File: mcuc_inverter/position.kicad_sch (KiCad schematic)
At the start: 0 parts

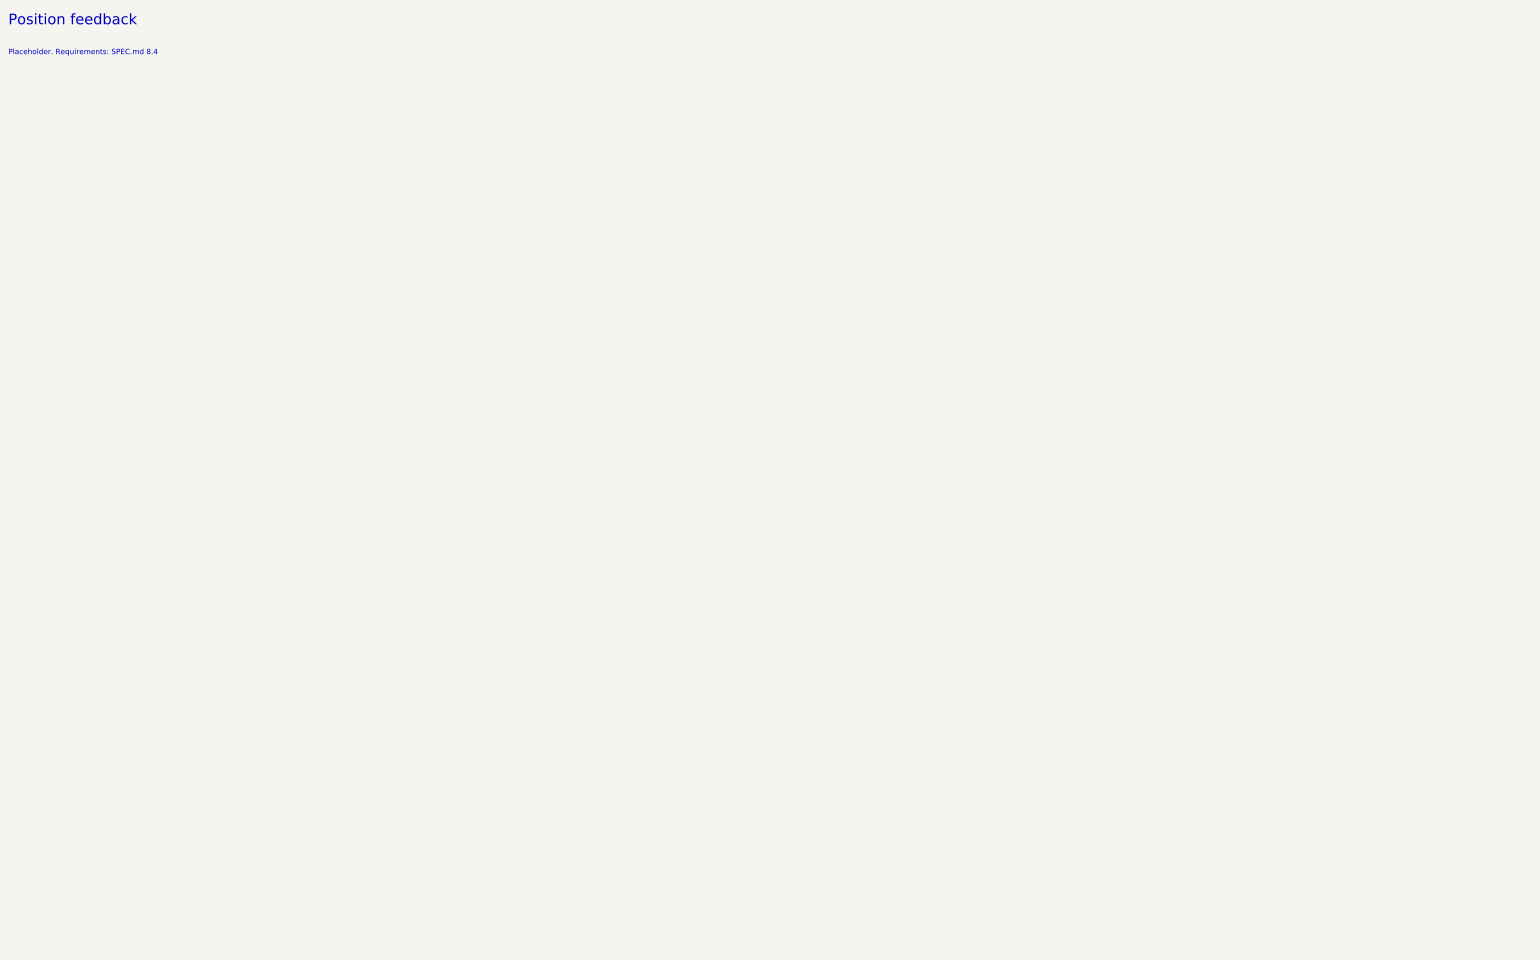
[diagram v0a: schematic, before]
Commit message: Capture position sheet: AD2S1205 resolver, halls, encoder, SinCos
Port from PALTA legacy sheets, verified pin-by-pin against the ADI
datasheet and the legacy VESC-controller.net (175/175 netlist
checks). Fixes two legacy defects found during reconstruction: SOE
(serial output enable, an INPUT mislabeled as output in the legacy
symbol) was left floating on PALTA - now tied low for serial mode;
and the A/B/NM encoder-emulation outputs that make VESC resolver
support free (D003) were never wired on the legacy board - now
brought out via 0R links with an exclusive-population note vs the
external ABI encoder. REFBYP decoupling added per datasheet (PALTA
floated pin 43).

Exciter (AD8397), hall clamps (10k + BAT54S, PALTA-faithful, DNP
pullup sites), encoder inputs replicating the hall pattern, SinCos
from the PALTA analog-input pattern, motor temp bias per D022
(resistor-selectable). APX809-46 5V supervisor for AD2S1205 RESET.
8 MHz -> 8.192 MHz crystal correction per datasheet nominal.

ERC 0 errors on root hierarchy.

Co-Authored-By: Claude Fable 5 <noreply@anthropic.com>
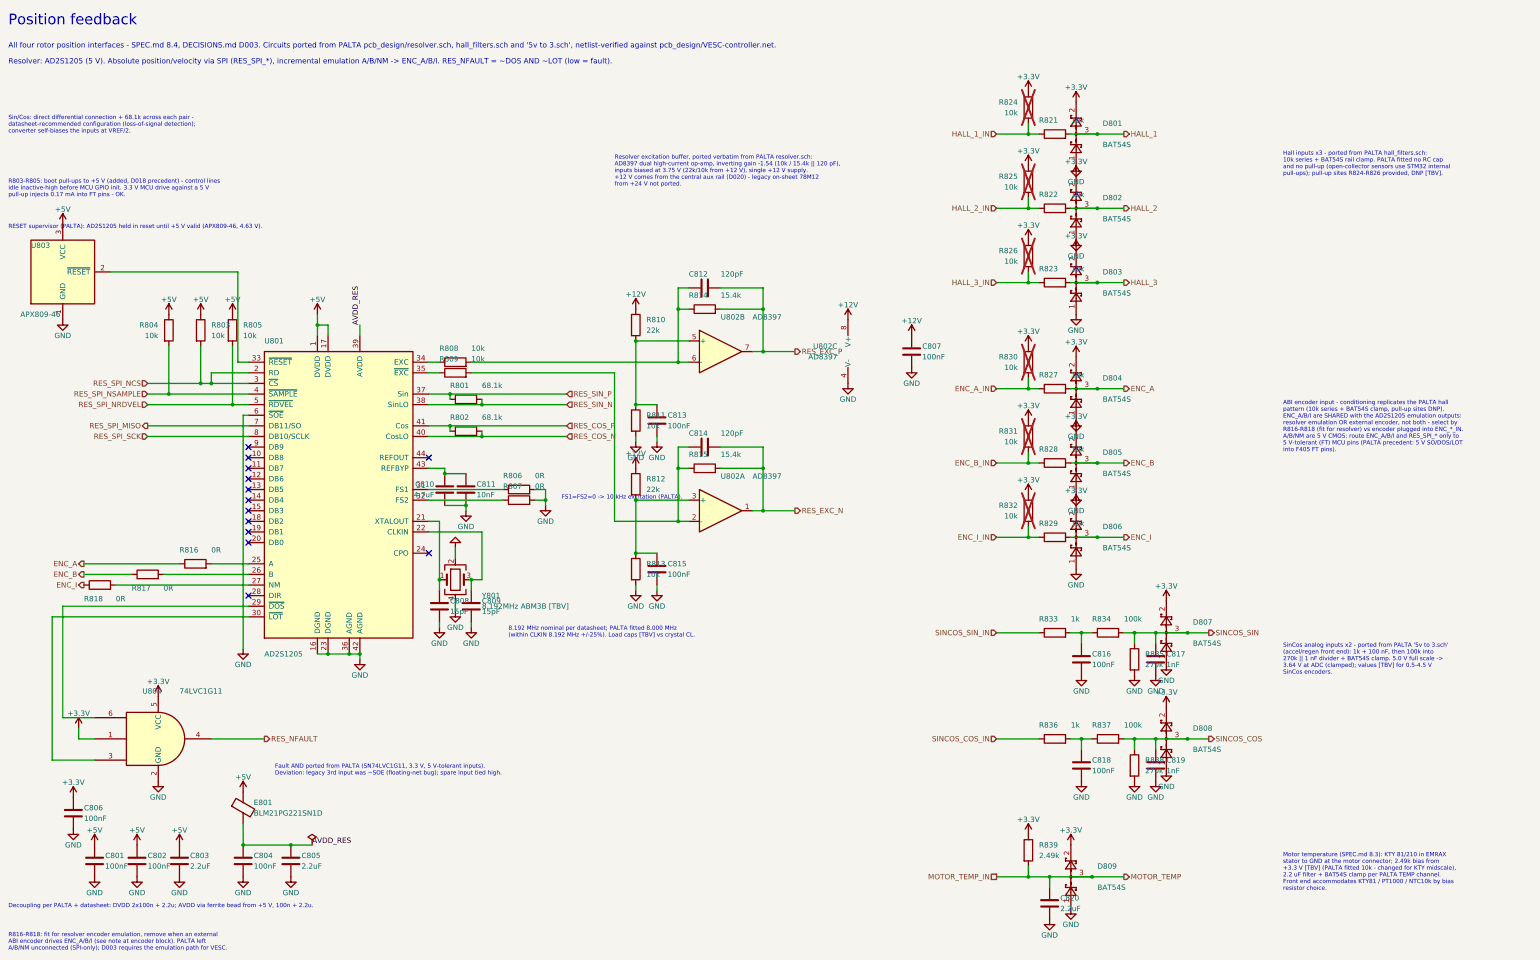
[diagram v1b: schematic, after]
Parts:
- added C801, C802, C804, C806, C807, C813, C815, C816, C818: 100nF, Capacitor_SMD:C_0603_1608Metric, symbol Device:C
- added C803, C805, C820: 2.2uF, Capacitor_SMD:C_0603_1608Metric, symbol Device:C
- added C808, C809: 15pF, Capacitor_SMD:C_0603_1608Metric, symbol Device:C
- added C810: 4.7uF, Capacitor_SMD:C_0603_1608Metric, symbol Device:C
- added C811: 10nF, Capacitor_SMD:C_0603_1608Metric, symbol Device:C
- added C812, C814: 120pF, Capacitor_SMD:C_0603_1608Metric, symbol Device:C
- added C817, C819: 1nF, Capacitor_SMD:C_0603_1608Metric, symbol Device:C
- added D801, D802, D803, D804, D805, D806, D807, D808, D809: BAT54S, Package_TO_SOT_SMD:SOT-23, symbol Diode:BAT54S
- added E801: BLM21PG221SN1D, Inductor_SMD:L_0805_2012Metric, symbol Device:FerriteBead
- added R801, R802: 68.1k, Resistor_SMD:R_0603_1608Metric, symbol Device:R
- added R803, R804, R805, R808, R809, R811, R813, R821, R822, R823, R824, R825, R826, R827, R828, R829, R830, R831, R832: 10k, Resistor_SMD:R_0603_1608Metric, symbol Device:R
- added R806, R807, R816, R817, R818: 0R, Resistor_SMD:R_0603_1608Metric, symbol Device:R
- added R810, R812: 22k, Resistor_SMD:R_0603_1608Metric, symbol Device:R
- added R814, R815: 15.4k, Resistor_SMD:R_0603_1608Metric, symbol Device:R
- added R833, R836: 1k, Resistor_SMD:R_0603_1608Metric, symbol Device:R
- added R834, R837: 100k, Resistor_SMD:R_0603_1608Metric, symbol Device:R
- added R835, R838: 270k, Resistor_SMD:R_0603_1608Metric, symbol Device:R
- added R839: 2.49k, Resistor_SMD:R_0603_1608Metric, symbol Device:R
- added U801: AD2S1205, Package_QFP:LQFP-44_10x10mm_P0.8mm, symbol mcuc:AD2S1205
- added U802: AD8397, Package_SO:SOIC-8_3.9x4.9mm_P1.27mm, symbol mcuc:AD8397
- added U803: APX809-46, Package_TO_SOT_SMD:SOT-23, symbol mcuc:APX809-46
- added U804: 74LVC1G11, Package_TO_SOT_SMD:SOT-363_SC-70-6, symbol 74xGxx:74LVC1G11
- added Y801: 8.192MHz ABM3B [TBV], Crystal:Crystal_SMD_Abracon_ABM3B-4Pin_5.0x3.2mm, symbol Device:Crystal_GND24
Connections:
- new net: C816.1, R833.2, R834.1
- new net: R818.2, U801.27 (NM)
- new net: C808.1, U801.21 (XTALOUT), Y801.1
- new net: C809.1, U801.22 (CLKIN), Y801.3
- new net: C813.1, R810.2, R811.1, U802.5 (+)
- new net: C812.1, R808.2, R814.1, U802.6 (-)
- new net: C814.1, R809.2, R815.1, U802.2 (-)
- new net: U801.30 (~{LOT}), U804.3
- new net: U801.29 (~{DOS}), U804.6
- new net: R816.2, U801.25 (A)
- new net: R817.2, U801.26 (B)
- new net: R806.1, U801.31 (FS1)
- new net: R807.1, U801.32 (FS2)
- new net: U801.33 (~{RESET}), U803.2 (~{RESET})
- new net: R808.1, U801.34 (EXC)
- new net: R809.1, U801.35 (~{EXC})
- new net: C810.1, C811.1, U801.43 (REFBYP)
- new net: C815.1, R812.2, R813.1, U802.3 (+)
- new net: C818.1, R836.2, R837.1
- new net +12V: C807.1, R810.1, R812.1, U802.8 (V+)
- new net +3.3V: C806.1, D801.2 (K), D802.2 (K), D803.2 (K), D804.2 (K), D805.2 (K), D806.2 (K), D807.2 (K), D808.2 (K), D809.2 (K), R824.1, R825.1, R826.1, R830.1, R831.1, R832.1, R839.1, U804.1, U804.5 (VCC)
- new net +5V: C801.1, C802.1, C803.1, E801.1, R803.1, R804.1, R805.1, U801.1 (DVDD), U801.17 (DVDD), U803.3 (VCC)
- new net AVDD_RES: C804.1, C805.1, E801.2, U801.39 (AVDD)
- new net ENC_A: D804.3 (COM), R816.1, R827.2
- new net ENC_A_IN: R827.1, R830.2
- new net ENC_B: D805.3 (COM), R817.1, R828.2
- new net ENC_B_IN: R828.1, R831.2
- new net ENC_I: D806.3 (COM), R818.1, R829.2
- new net ENC_I_IN: R829.1, R832.2
- new net GND: C801.2, C802.2, C803.2, C804.2, C805.2, C806.2, C807.2, C808.2, C809.2, C810.2, C811.2, C813.2, C815.2, C816.2, C817.2, C818.2, C819.2, C820.2, D801.1 (A), D802.1 (A), D803.1 (A), D804.1 (A), D805.1 (A), D806.1 (A), D807.1 (A), D808.1 (A), D809.1 (A), R806.2, R807.2, R811.2, R813.2, R835.2, R838.2, U801.16 (DGND), U801.23 (DGND), U801.36 (AGND), U801.42 (AGND), U801.6 (~{SOE}), U802.4 (V-), U803.1 (GND), U804.2 (GND), Y801.2, Y801.4
- new net HALL_1: D801.3 (COM), R821.2
- new net HALL_1_IN: R821.1, R824.2
- new net HALL_2: D802.3 (COM), R822.2
- new net HALL_2_IN: R822.1, R825.2
- new net HALL_3: D803.3 (COM), R823.2
- new net HALL_3_IN: R823.1, R826.2
- new net MOTOR_TEMP: C820.1, D809.3 (COM), R839.2
- new net RES_COS_N: R802.2, U801.40 (CosLO)
- new net RES_COS_P: R802.1, U801.41 (Cos)
- new net RES_EXC_N: C814.2, R815.2, U802.1
- new net RES_EXC_P: C812.2, R814.2, U802.7
- new net RES_NFAULT: U804.4
- new net RES_SIN_N: R801.2, U801.38 (SinLO)
- new net RES_SIN_P: R801.1, U801.37 (Sin)
- new net RES_SPI_MISO: U801.7 (DB11/SO)
- new net RES_SPI_NCS: R803.2, U801.2 (RD), U801.3 (~{CS})
- new net RES_SPI_NRDVEL: R805.2, U801.5 (~{RDVEL})
- new net RES_SPI_NSAMPLE: R804.2, U801.4 (~{SAMPLE})
- new net RES_SPI_SCK: U801.8 (DB10/SCLK)
- new net SINCOS_COS: C819.1, D808.3 (COM), R837.2, R838.1
- new net SINCOS_COS_IN: R836.1
- new net SINCOS_SIN: C817.1, D807.3 (COM), R834.2, R835.1
- new net SINCOS_SIN_IN: R833.1
- no-connect marks 0 -> 13
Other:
- note added: "8.192 MHz nominal per datasheet; PALTA fitted 8.000 MHz (within CLKIN 8.192 MHz +/-25%). Load caps [TBV] vs crystal CL."
- note added: "ABI encoder input - conditioning replicates the PALTA hall pattern (10k series + BAT54S clamp, pull-up sites DNP). ENC_A/B/I are SHARED with the AD2S1205 emulation outputs: resolver emulation OR external encoder, not both - select by R816-R818 (fit for resolver) vs encoder plugged into ENC_*_IN. A/B/NM are 5 V CMOS: route ENC_A/B/I and RES_SPI_* only to 5 V-tolerant (FT) MCU pins (PALTA precedent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"
- note added: "All four rotor position interfaces - SPEC.md 8.4, DECISIONS.md D003. Circuits ported from PALTA pcb_design/resolver.sch, hall_filters.sch and '5v to 3.sch', netlist-verified against pcb_design/VESC-controller.net."
- note added: "Decoupling per PALTA + datasheet: DVDD 2x100n + 2.2u; AVDD via ferrite bead from +5 V, 100n + 2.2u."
- note added: "FS1=FS2=0 -> 10 kHz excitation (PALTA)."
- note added: "Fault AND ported from PALTA (SN74LVC1G11, 3.3 V, 5 V-tolerant inputs). Deviation: legacy 3rd input was ~SOE (floating-net bug); spare input tied high."
- note added: "Hall inputs x3 - ported from PALTA hall_filters.sch: 10k series + BAT54S rail clamp. PALTA fitted no RC cap and no pull-up (open-collector sensors use STM32 internal pull-ups); pull-up sites R824-R826 provided, DNP [TBV]."
- note added: "Motor temperature (SPEC.md 8.3): KTY 81/210 in EMRAX stator to GND at the motor connector; 2.49k bias from +3.3 V [TBV] (PALTA fitted 10k - changed for KTY midscale), 2.2 uF filter + BAT54S clamp per PALTA TEMP channel. Front end accommodates KTY81 / PT1000 / NTC10k by bias resistor choice."
- note added: "R803-R805: boot pull-ups to +5 V (added, D018 precedent) - control lines idle inactive-high before MCU GPIO init. 3.3 V MCU drive against a 5 V pull-up injects 0.17 mA into FT pins - OK."
- note added: "R816-R818: fit for resolver encoder emulation, remove when an external ABI encoder drives ENC_A/B/I (see note at encoder block). PALTA left A/B/NM unconnected (SPI-only); D003 requires the emulation path for VESC."
- note added: "RESET supervisor (PALTA): AD2S1205 held in reset until +5 V valid (APX809-46, 4.63 V)."
- note added: "Resolver excitation buffer, ported verbatim from PALTA resolver.sch: AD8397 dual high-current op-amp, inverting gain -1.54 (10k / 15.4k || 120 pF), inputs biased at 3.75 V (22k/10k from +12 V), single +12 V supply. +12 V comes from the central aux rail (D020) - legacy on-sheet 78M12 from +24 V not ported."
- note added: "Resolver: AD2S1205 (5 V). Absolute position/velocity via SPI (RES_SPI_*), incremental emulation A/B/NM -> ENC_A/B/I. RES_NFAULT = ~DOS AND ~LOT (low = fault)."
- note added: "Sin/Cos: direct differential connection + 68.1k across each pair - datasheet-recommended configuration (loss-of-signal detection); converter self-biases the inputs at VREF/2."
- note added: "SinCos analog inputs x2 - ported from PALTA '5v to 3.sch' (accel/regen front end): 1k + 100 nF, then 100k into 270k || 1 nF divider + BAT54S clamp. 5.0 V full scale -> 3.64 V at ADC (clamped); values [TBV] for 0.5-4.5 V SinCos encoders."
- note removed: "Placeholder. Requirements: SPEC.md 8.4"

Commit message: Wire full MCU pin map; add verified PINOUT.md
All 33 remaining signals wired per the citation-verified map (D023):
phase currents PC0/1/2 on VESC triple-simultaneous ADC channels,
V_BUS PC3, temps PA3/PB0/PC4, SinCos PA5/PA6, I_REF PA4/PA7/PB1,
encoder PC6/7/8 (TIM3), halls PD12/13/14, resolver SPI3 PC10/PC11 +
PA15 boot-safe CS + PD0/PD1/PD2 controls, supervisor GPIOs PD3/4/5,
precharge/contactor/discharge PE2/3/4, LED PE0, VBUS sense PC5, PPM
PB6 (TIM4_CH1, VESC convention - repurposed J1206 spare pin).
PA0/1/2 and PB10/11 reserved with on-sheet notes.

AD2S1205 drive validated in-datasheet: VIH 2.0 V @ 5 V supply, so
3.3 V MCU outputs are legal; its 5 V outputs land on FT pins only.

docs/PINOUT.md: complete table with per-row DS8626 Table 7/9
citations, 5V-tolerance column with the analog-mode caveat, and the
D023 reservations - generated against the post-wiring netlist.

ERC 0 errors (warnings down 224 -> 201 as dangling pins connected).
33/33 nets machine-verified U1-pad-to-counterpart; 6 re-verified
independently before commit.

Co-Authored-By: Claude Fable 5 <noreply@anthropic.com>
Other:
- note added: "AD2S1205 digital inputs: VIH min = 2.0 V at VDD = 5 V (datasheet Electrical Characteristics) - 3.3 V MCU drive on RES_SPI_SCK/NCS/NSAMPLE/NRDVEL verified."
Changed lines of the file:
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@@
+		)
+	)
+	(text "AD2S1205 digital inputs: VIH min = 2.0 V at VDD = 5 V\n(datasheet Electrical Characteristics) - 3.3 V MCU drive\non RES_SPI_SCK/NCS/NSAMPLE/NRDVEL verified."
+		(exclude_from_sim no)
+		(at 20 132.08 0)
+		(effects
+			(font
+				(size 1.27 1.27)
+			)
+			(justify left bottom)
 		)
 	)

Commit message: Board-prep: footprint audit complete, HV terminals, off-board flags
474-component audit: 466 valid resolved footprints, 13 off-board
exclusions per D024 (caps to carrier, chassis resistors, HOYS), 4
flagged TBDs (custom flyback + 3 unchosen inductors), zero silent
gaps. Netlist-fatal fixes: Q403 renumbered to Wolfspeed TO-263-7
convention (G1/KS2/S3-7/tab-D8), CSD18543Q3A remapped to KiCad's
SSSGD VSON-8 pairing - both verified in the netlist afterward.

New HV interface terminals J401-J405 (M4 ring-lug pads: DC input,
precharge-R chassis loop, discharge-R return, bus taps) and HOYS
harness headers J501-J503 (JST 2mm; PA-vs-PH footprint flagged TBV)
with net membership machine-verified incl. the OC_TRIP wire-OR and
I_REF paths to the MCU ADCs.

ERC 0 errors, warnings 201 -> 200 (none introduced).

Co-Authored-By: Claude Fable 5 <noreply@anthropic.com>
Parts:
- U802: footprint Package_SO:SOIC-8_3.9x4.9mm_P1.27mm -> Package_SO:SOIC-8-1EP_3.9x4.9mm_P1.27mm_EP2.29x3mm
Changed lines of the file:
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@@
 			)
 		)
-		(property "Footprint" "Package_SO:SOIC-8_3.9x4.9mm_P1.27mm"
+		(property "Footprint" "Package_SO:SOIC-8-1EP_3.9x4.9mm_P1.27mm_EP2.29x3mm"
 			(at 190.5 97.79 0)
 			(effects
@@
 			)
 		)
-		(property "Footprint" "Package_SO:SOIC-8_3.9x4.9mm_P1.27mm"
+		(property "Footprint" "Package_SO:SOIC-8-1EP_3.9x4.9mm_P1.27mm_EP2.29x3mm"
 			(at 190.5 135.89 0)
 			(effects
@@
 			)
 		)
-		(property "Footprint" "Package_SO:SOIC-8_3.9x4.9mm_P1.27mm"
+		(property "Footprint" "Package_SO:SOIC-8-1EP_3.9x4.9mm_P1.27mm_EP2.29x3mm"
 			(at 223.52 97.79 0)
 			(effects

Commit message: Fix precharge, current sense, position, comms per review
Also repairs a library-breaking defect the agent found while working:
the VOM1271T symbol contained a raw newline inside a quoted string,
which silently truncated mcuc_inverter.kicad_sym at parse - every
symbol defined after it was unresolvable. That had been latent since
the symbol was written.

MJ-2/3 - the comparators were wrong twice over: TLV7032 is push-pull
(six of them wire-ORed together plus three open-drain transducer OCD
pins is direct contention), and LM2903's input common-mode range on
3.3 V stops at 1.8 V, below the 2.34 V upper threshold, so the
over-current half could never trip. Now TLV7022DDFR: true open-drain,
rail-to-rail input, 260 ns instead of ~3 us.

MJ-4 - the trip point was really 245-356 A because the thresholds
rode a +-4% rail while the transducer's reference is absolute. Each
phase's window is now servo'd off its own Uref through an OPA376
buffer, so the threshold tracks the sensor: 300 A +-8 A.

MJ-7 - a harness disconnect was not fail-safe: that phase's OCD left
the wire-OR and the input floated. 100k pull-downs make an open
harness read as a large negative current and latch the trip at
power-up, before HV is applied.

MJ-12 - the active discharge can no longer be commanded into a live
bus: SN74LVC1G97 computes DISCHARGE_EN AND NOT(CONTACTOR_EN)
self-contained on the sheet, plus a 10k boot pull-down.

Discharge gate now has a real Miller clamp (BSS138 + 1n + 10k) firing
at V_GS ~1.34 V, below the FET's 1.8 V threshold, in under 15 ns -
the 450 V dv/dt step could previously inject ~4.4 V against a 10M
pull-down and a uA-class photovoltaic turn-off.

Bleeder 18.7k -> 14k (56 k total, 56.4 s to 60 V, meeting the <60 s
requirement it was failing at 75.4 s). Precharge resistor respec'd to
>=65 J. Coil freewheels upsized to ES1G/ES2G with anti-series SMBJ24A
TVS for fast relay release, which forced the coil drivers to 60 V
parts - documented with a 17% margin note.

Position: SinCos f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
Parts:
- added R840: 1.00k, Resistor_SMD:R_0603_1608Metric, symbol Device:R
- added R841: 10.0k, Resistor_SMD:R_0603_1608Metric, symbol Device:R
- C816, C818: value 100nF -> 1nF
- R816, R817, R818: value 0R -> 1k
- R834, R837: value 100k -> 10k
- R835, R838: value 270k -> 27k
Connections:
- net +3.3V: now also R840.1, R841.1
- net MOTOR_TEMP: now also R840.2, R841.2
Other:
- note added: "Motor temperature (SPEC 8.3 / D022, review 3 MN-11). The EMRAX KTY 81/210 is obsolete (NXP EOL 2020) and SPEC 8.3 / D022 promise a RESISTOR-SELECTABLE front end covering PT1000 / KTY8x / NTC 10k. The sheet previously had only the fixed 2.49k, so that claim was not implemented. Three parallel bias positions from +3.3 V are now provided - FIT EXACTLY ONE: R839 2.49k FITTED - KTY 81/210 or KTY83/84 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"
- note added: "R816-R818 = 1k (was 0R - review 3 MN-3). The AD2S1205 A/B/NM outputs are 5 V CMOS (V_OH min 4.0 V at VDD 5 V) and ENC_A/B/I are clamped to +3.3 V by D804-D806 (BAT54S). At 0R the clamp current was bounded only by the driver's own output impedance; 1k limits it to (5.0 - 3.6)/1k = 1.4 mA, inside BAT54S I_F(AV) 200 mA, and still drives the ~10 pF MCU pin with a 10 ns time constant. Fit for resolver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"
- note added: "SinCos analog inputs x2 - PALTA '5v to 3.sch' topology, RESCALED for rotor-position bandwidth (review 3 MJ-15). The legacy accel/regen values (1k + 100 nF, 100k / 270k || 1 nF) gave a 1.59 kHz first pole and a 73.0 kOhm ADC source impedance: ~71 deg of electrical lag at 8000 rpm on a 10-pole-pair motor (f_e = 1333 Hz) - unusable for FOC. Now: R833/R836 1k + C816/C818 1 nF -> pole 159 kHz (0.48 de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"
- note removed: "Motor temperature (SPEC.md 8.3): KTY 81/210 in EMRAX stator to GND at the motor connector; 2.49k bias from +3.3 V [TBV] (PALTA fitted 10k - changed for KTY midscale), 2.2 uF filter + BAT54S clamp per PALTA TEMP channel. Front end accommodates KTY81 / PT1000 / NTC10k by bias resistor choice."
- note removed: "R816-R818: fit for resolver encoder emulation, remove when an external ABI encoder drives ENC_A/B/I (see note at encoder block). PALTA left A/B/NM unconnected (SPI-only); D003 requires the emulation path for VESC."
- note removed: "SinCos analog inputs x2 - ported from PALTA '5v to 3.sch' (accel/regen front end): 1k + 100 nF, then 100k into 270k || 1 nF divider + BAT54S clamp. 5.0 V full scale -> 3.64 V at ADC (clamped); values [TBV] for 0.5-4.5 V SinCos encoders."
